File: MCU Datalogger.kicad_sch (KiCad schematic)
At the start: 25 parts, among them U1 24LC1025, U2 24LC1025, U3 DS1337S_, U4 ATMEGA328P-AU, Y1 16 MHz, Y2 32.768kHz

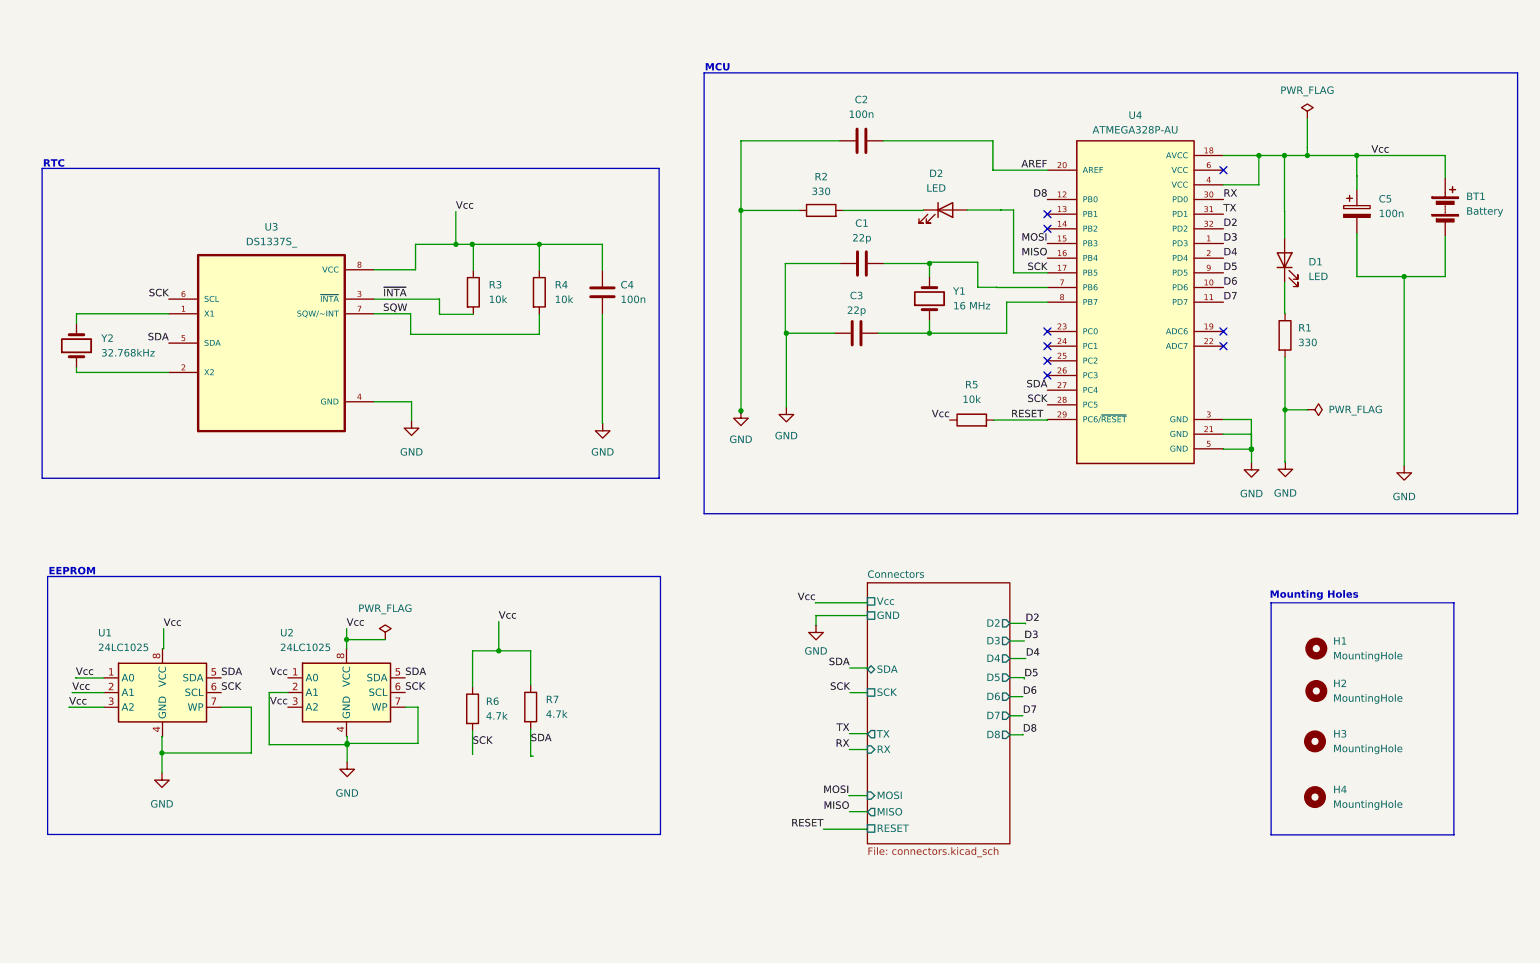
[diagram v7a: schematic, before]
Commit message: Fixed two defects in the schematic
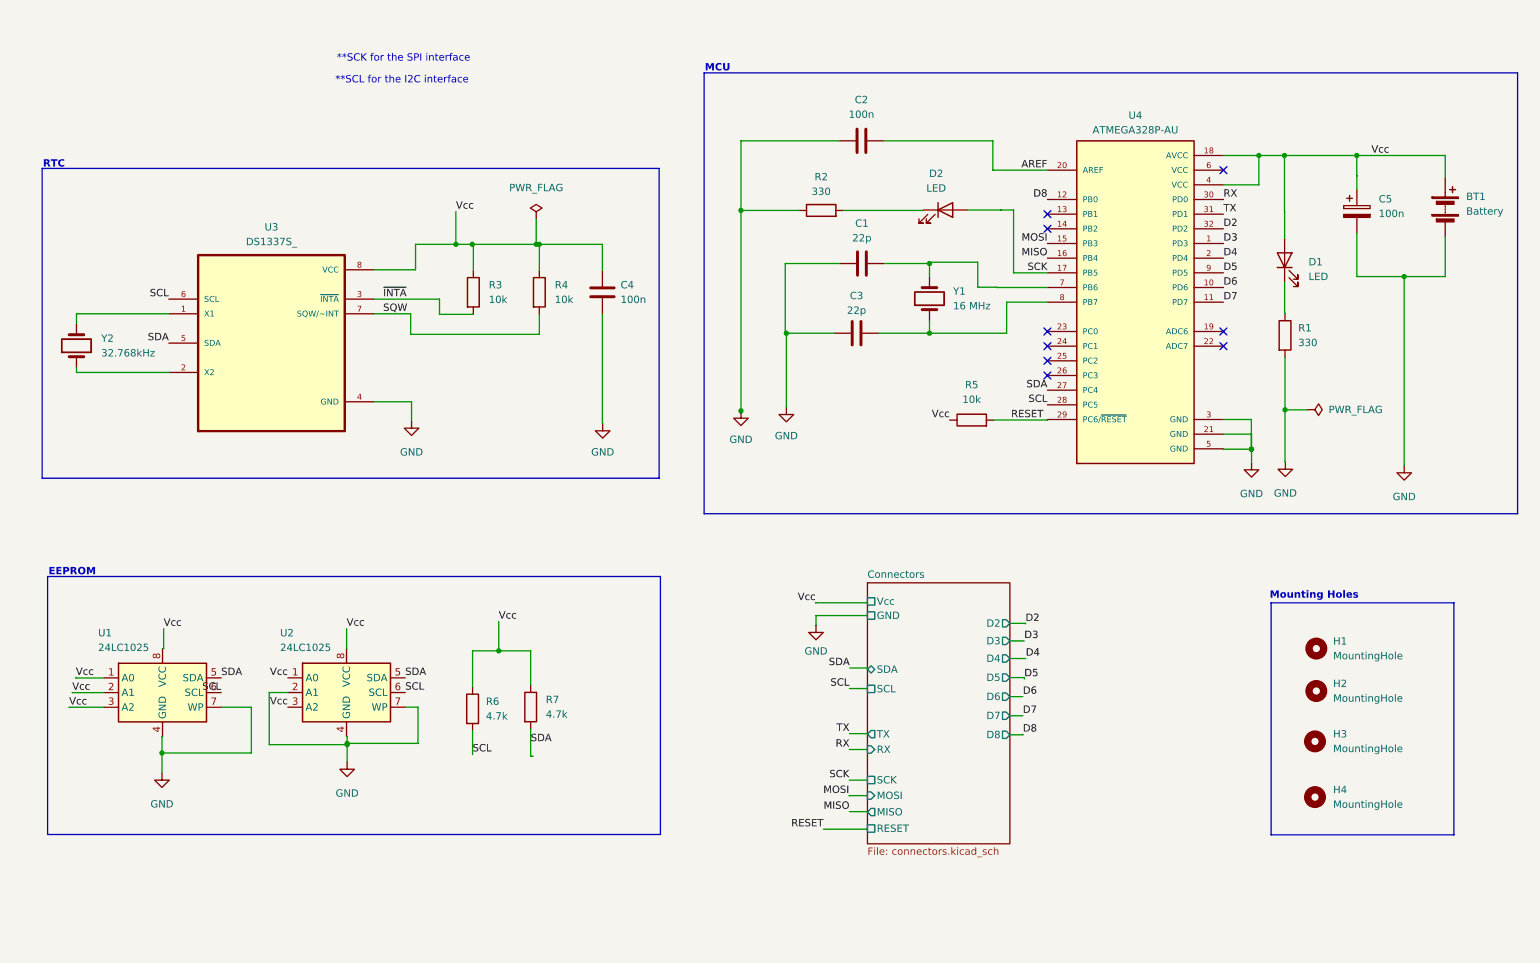
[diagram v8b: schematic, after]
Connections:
- net SCK: no longer R6.2, U1.6 (SCL), U2.6 (SCL), U3.6 (SCL), U4.28 (PC5)
- new net SCL: R6.2, U1.6 (SCL), U2.6 (SCL), U3.6 (SCL), U4.28 (PC5)
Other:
- sheet Connectors ports: added SCL; removed none
- note added: "**SCK for the SPI interface"
- note added: "**SCL for the I2C interface"
